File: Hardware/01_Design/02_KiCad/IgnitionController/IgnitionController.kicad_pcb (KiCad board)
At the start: 4 copper layers, 227 parts, among them J1 770669-1, J2 Conn_02x03_Odd_Even, J3 FTSH-105-01-L-DV-A, Q1 SS8050, Q10 IRF540N, Q11 IRF540N, Q12 IRF540N, Q13 IRF540N, Q14 IRF540N, Q15 IRF540N, Q2 DMP6050SSD, Q3 DMP6050SSD, Q4 RSJ250P10FRATL, Q5 BC856, Q6 942-IRF9Z34NSPBF, Q7 SS8050, Q8 IRF540N, Q9 IRF540N, U1 ATmega328PB-A, U10 TLV2372, U11 TLV2372, U12 STM32F407VGTx, U13 TLV2372, U14 AT24CS01-SSHM, U15 MCP2557FD-xSN, U16 MAX232, U19 IXDN602, U2 4N35, U20 IXDN602, U21 IXDN602, U22 IXDN602, U23 4N35, U24 4N35, U25 TXS0104EPW, U3 LM2575-3.3BU, U4 LM2575-5.0BU, U5 4N35, U6 4N35, U7 4N35, U8 TXS0104EPW, U9 LM2575-5.0BU, Y1 FL0800011Q, Y3 XT1312HHRXX32K76E, Y4 NX2016SA-16MHZ-EXS00A-CS07826

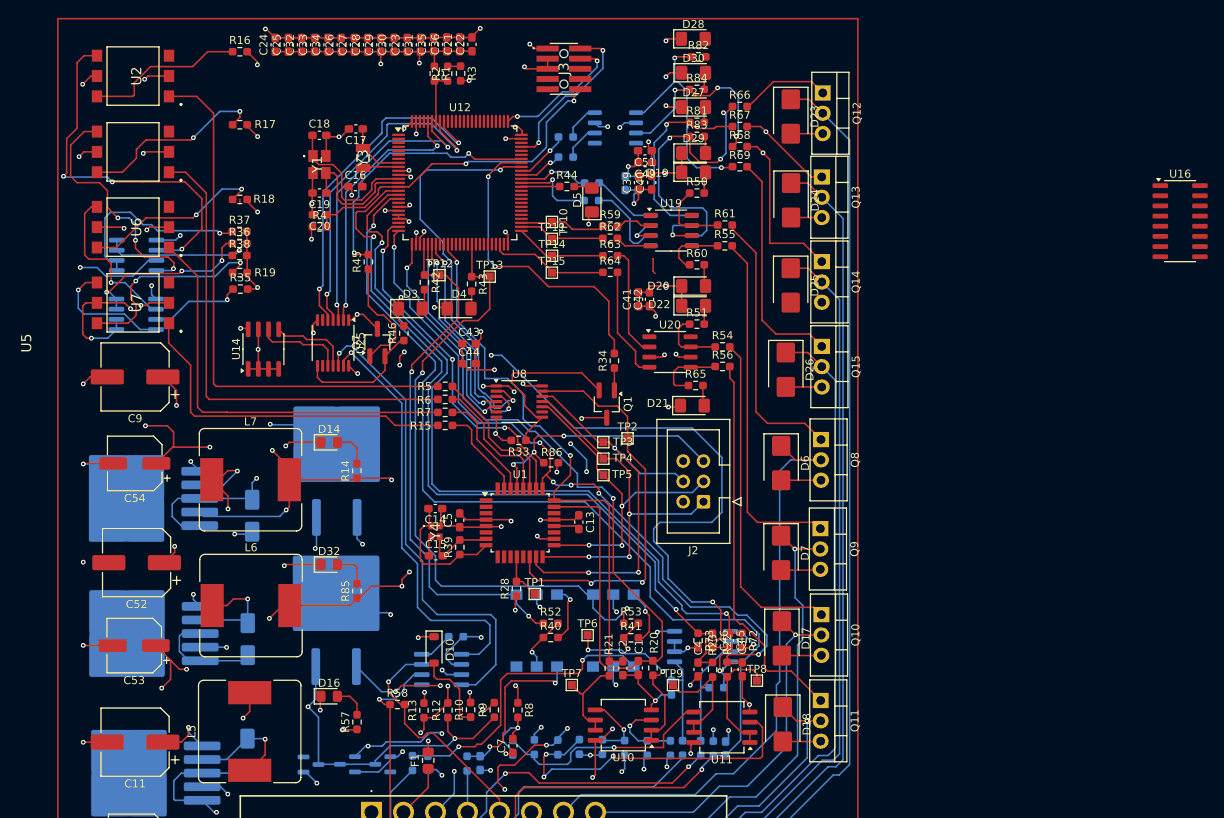
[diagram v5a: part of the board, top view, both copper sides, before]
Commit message: Updated Solder Mask labels
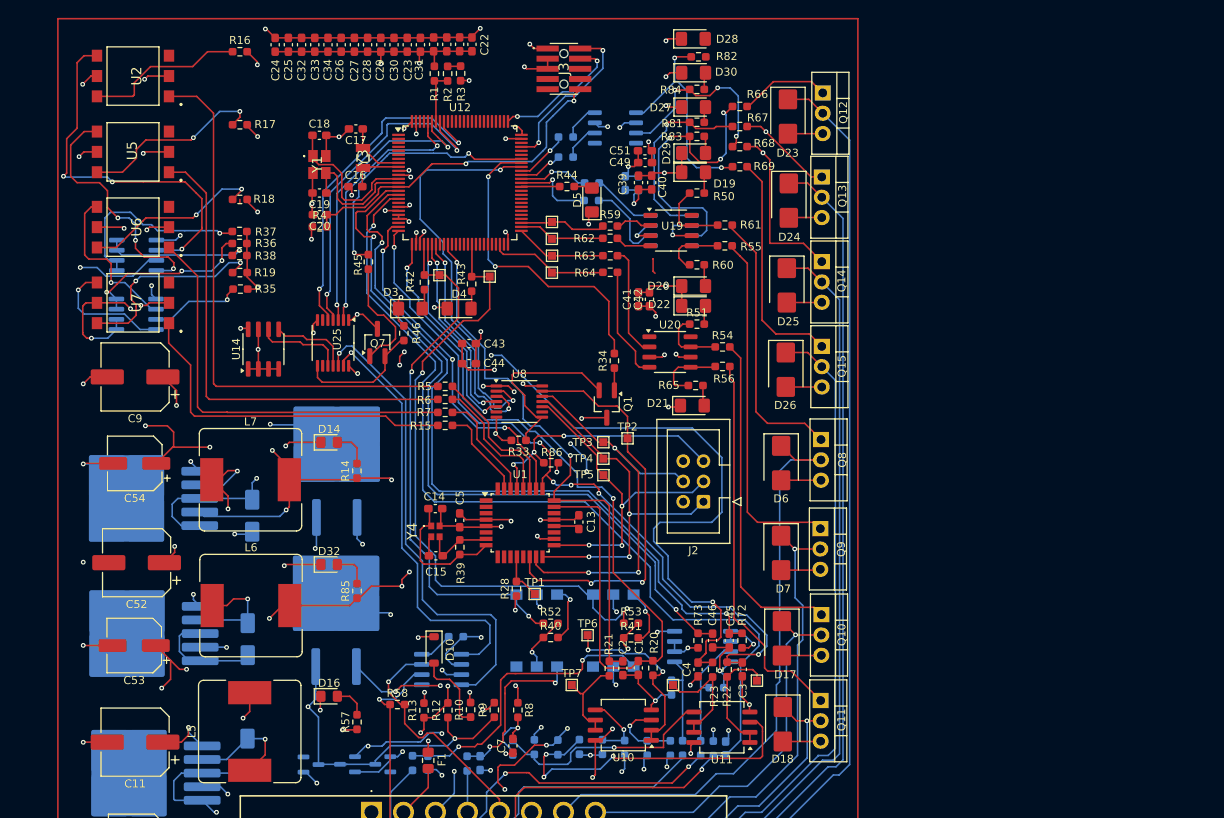
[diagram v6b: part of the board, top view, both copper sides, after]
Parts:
- removed U16: MAX232, Package_SO:SOIC-16_3.9x9.9mm_P1.27mm
- moved D25 0.48 mm to (158.0, 63.3)
- moved D23 0.35 mm to (158.2, 42.2)
- moved D24 0.28 mm to (158.3, 52.7)
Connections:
- J1 pad 18: UART_TX -> unconnected-(J1-Pad18)
- J1 pad 6: UART_RX -> unconnected-(J1-Pad6)
- R72 pad 1: MAP_SENSOR_ADC_SIGNAL -> Net-(U13A--)
- R72 pad 2: Net-(U13A--) -> MAP_SENSOR_ADC_SIGNAL
- R73 pad 1: TPS_ADC_SIGNAL -> Net-(U13B--)
- R73 pad 2: Net-(U13B--) -> TPS_ADC_SIGNAL
- R81 pad 1: FUEL_INJ_DRV_2 -> Net-(D27-A)
- R81 pad 2: Net-(D27-A) -> Net-(U21-OUTB)
- U12 pad 78: UART_TX -> unconnected-(U12-PC10-Pad78)
- U12 pad 79: UART_RX -> unconnected-(U12-PC11-Pad79)
- U21 pad 5: FUEL_INJ_DRV_2 -> Net-(U21-OUTB)
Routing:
- net GND: track 1096.0 -> 1100.4 mm

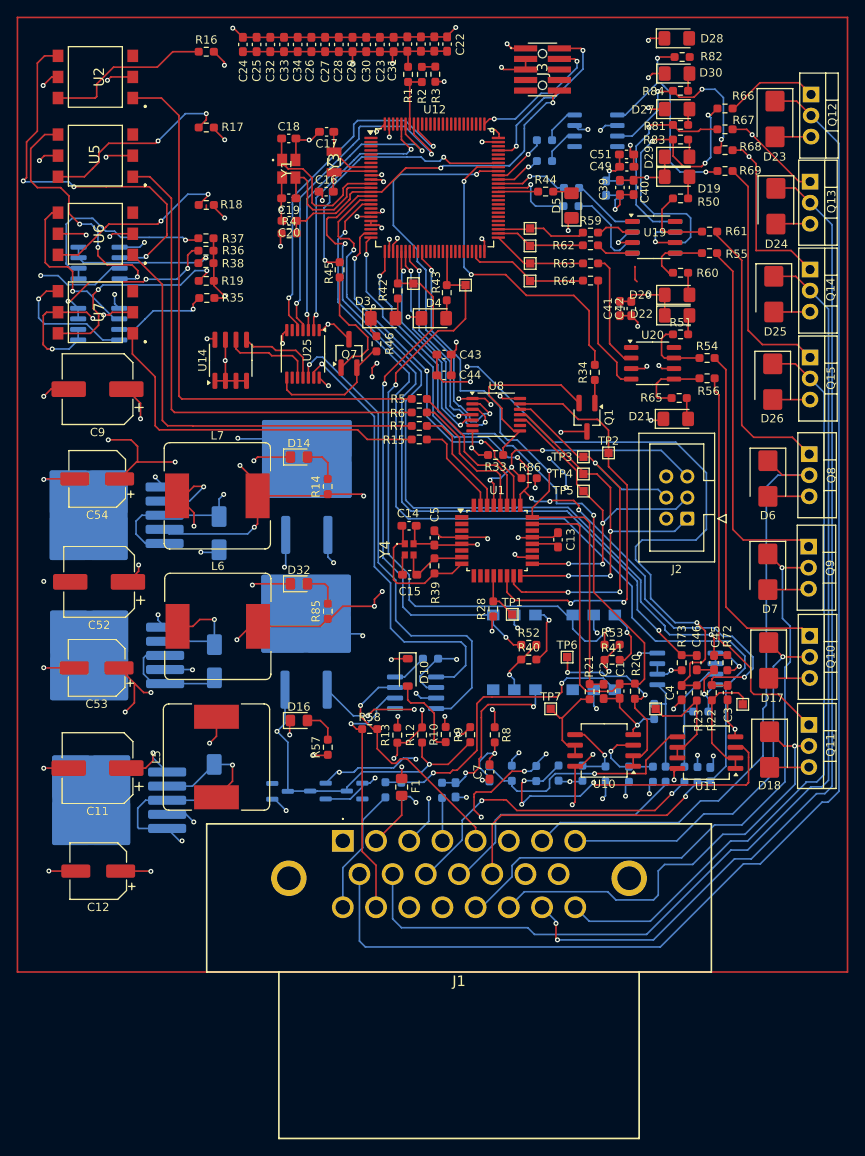
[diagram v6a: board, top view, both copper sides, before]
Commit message: Addition of 3d model of ECU
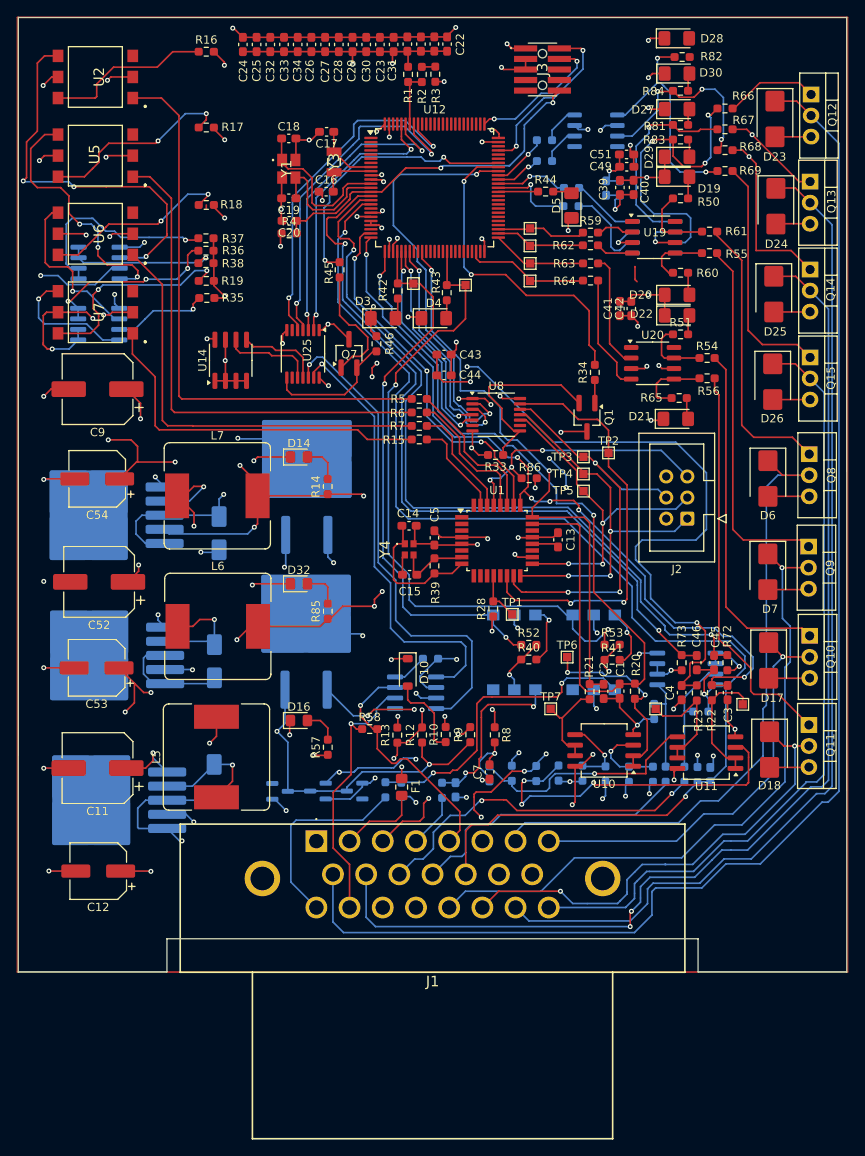
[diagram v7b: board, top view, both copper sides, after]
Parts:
- moved J1 3.19 mm to (102.9, 129.2)
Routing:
- net SENSOR_2_SIGNAL: track 15.4 -> 24.0 mm
- net GND: track 1100.4 -> 1092.2 mm
- net INJ_FUEL_3: track 130.9 -> 135.5 mm, vias 0 -> 2
- net IGN_COIL_1: track 74.9 -> 78.8 mm
- net TPS_SIGNAL: track 31.3 -> 34.5 mm
- net +BATT: track 6.74 -> 9.94 mm
- net IGN_COIL_3: track 47.4 -> 50.6 mm
- net IGN_COIL_4: track 53.2 -> 56.3 mm, vias 1 -> 2
- net MAP_SENSOR_SIGNAL: track 38.2 -> 41.2 mm
- net INJ_FUEL_4: track 91.7 -> 94.5 mm
- net COOLANT_TEMP_ADC_SIGNAL: track 146.0 -> 148.8 mm
- net VSEN: track 164.6 -> 162.1 mm
- net IGN_COIL_2: track 76.4 -> 78.9 mm
- net INJ_FUEL_1: track 161.4 -> 163.5 mm
- net VPMIC: track 265.6 -> 263.7 mm
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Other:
- board outline added: 99.8 x 115 mm
